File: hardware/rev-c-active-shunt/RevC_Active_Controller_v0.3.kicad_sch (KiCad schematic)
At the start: 17 parts, among them J1 TEST_A / GND, J2 +12/GND/-12, U1 OPA551PA

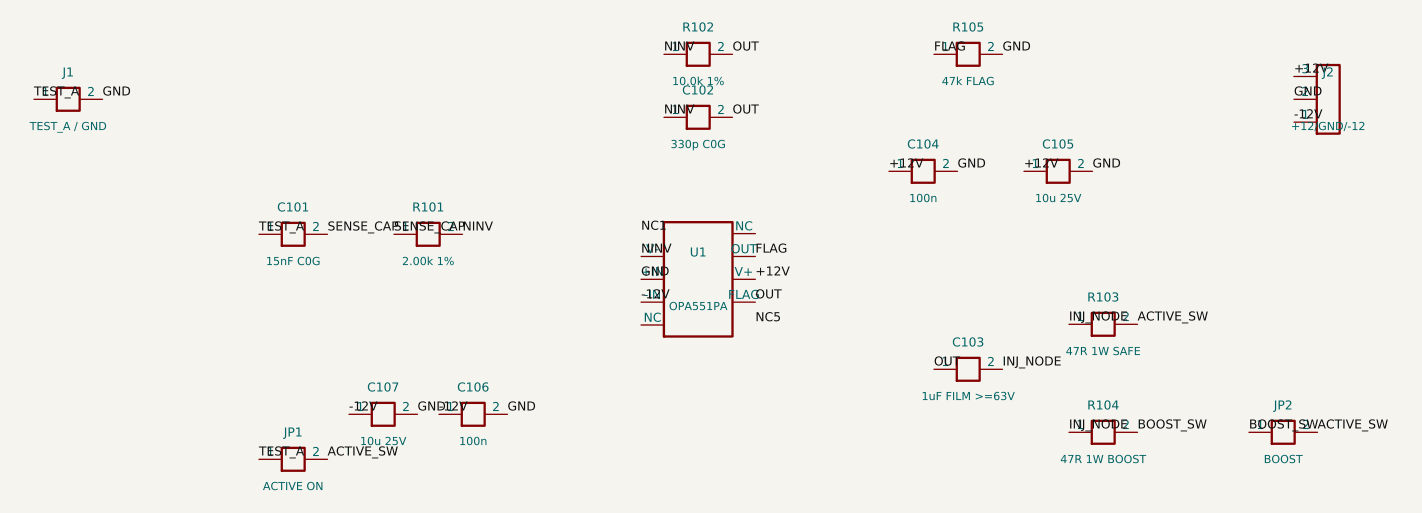
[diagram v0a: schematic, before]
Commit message: Rev.C v0.3.1: fix pin mapping, parity, libraries, and PCB routing
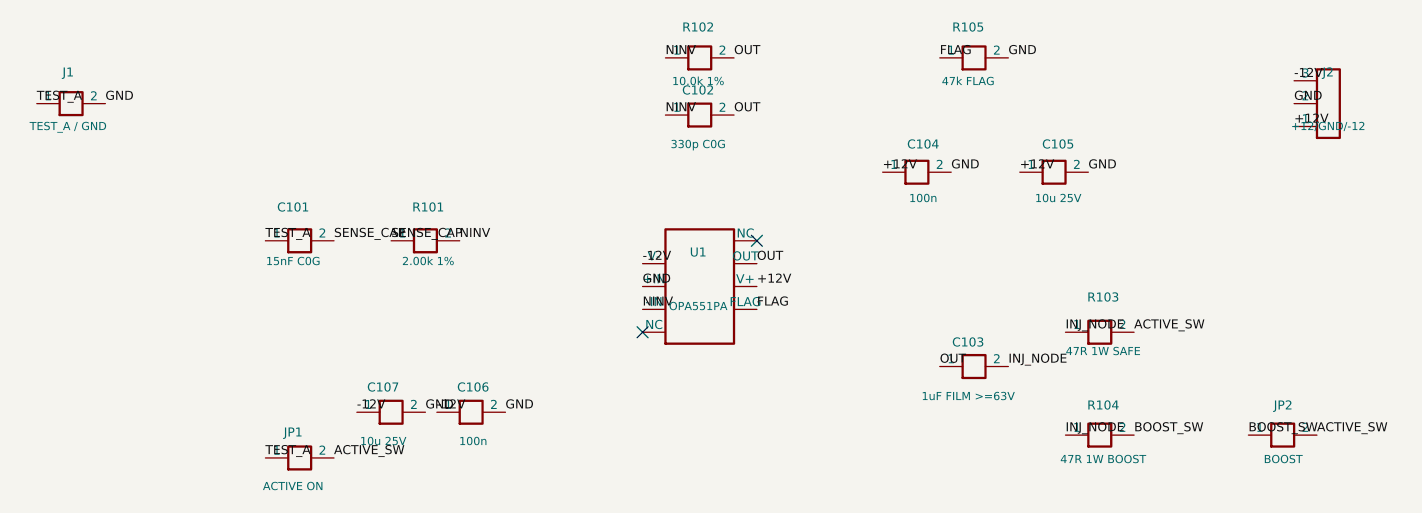
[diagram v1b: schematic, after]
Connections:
- net +12V: now also J2.1; no longer J2.3
- net -12V: now also J2.3, U1.4 (V-); no longer J2.1, U1.2 (-IN)
- net FLAG: now also U1.8 (FLAG); no longer U1.6 (OUT)
- net NINV: now also U1.2 (-IN); no longer U1.4 (V-)
- net OUT: now also U1.6 (OUT); no longer U1.8 (FLAG)
- no-connect marks 0 -> 2
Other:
- moved on the sheet: C101, C103, C104, C107, J1, JP1, R101, R103, R105, U1
